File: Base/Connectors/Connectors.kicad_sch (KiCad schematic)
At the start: 18 parts, among them J1 Barrel_Jack_Switch, J2 AudioJack2_Ground, J3 AudioJack2_Ground, J4 RJ45_LED_Shielded, J5 USB_C_Receptacle_USB2.0_16P, Q1 40V

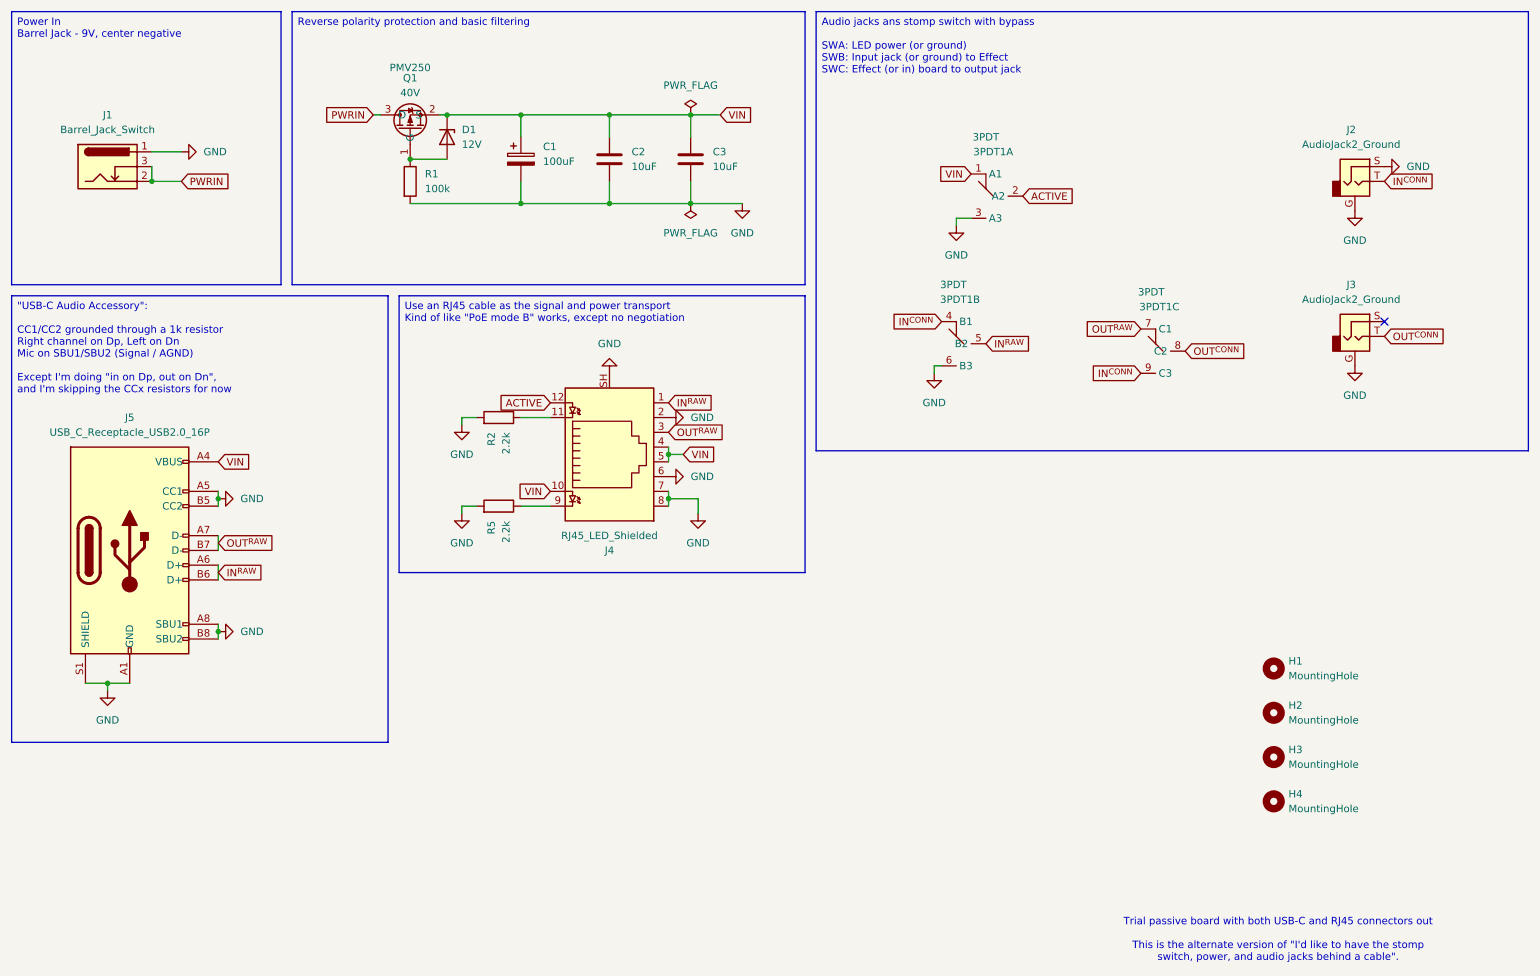
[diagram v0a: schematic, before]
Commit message: Simplify the connector testing to just a USB-C connector
This is mainly to see what that would look like, particularly for the
base that now becomes really simple and small.

The effect connector ends up being crazy large just because of the old
pin header layout.  But the point of all this is that if it works out,
we'll dispense with the pin headers, and just use the USB-C connector
"natively".

So the effects board is just a temporary thing, and the base board is
where it's at.  If the base board works well, and I can stop soldering
stomp switches, I'll be good.

Signed-off-by: Linus Torvalds <torvalds@linux-foundation.org>
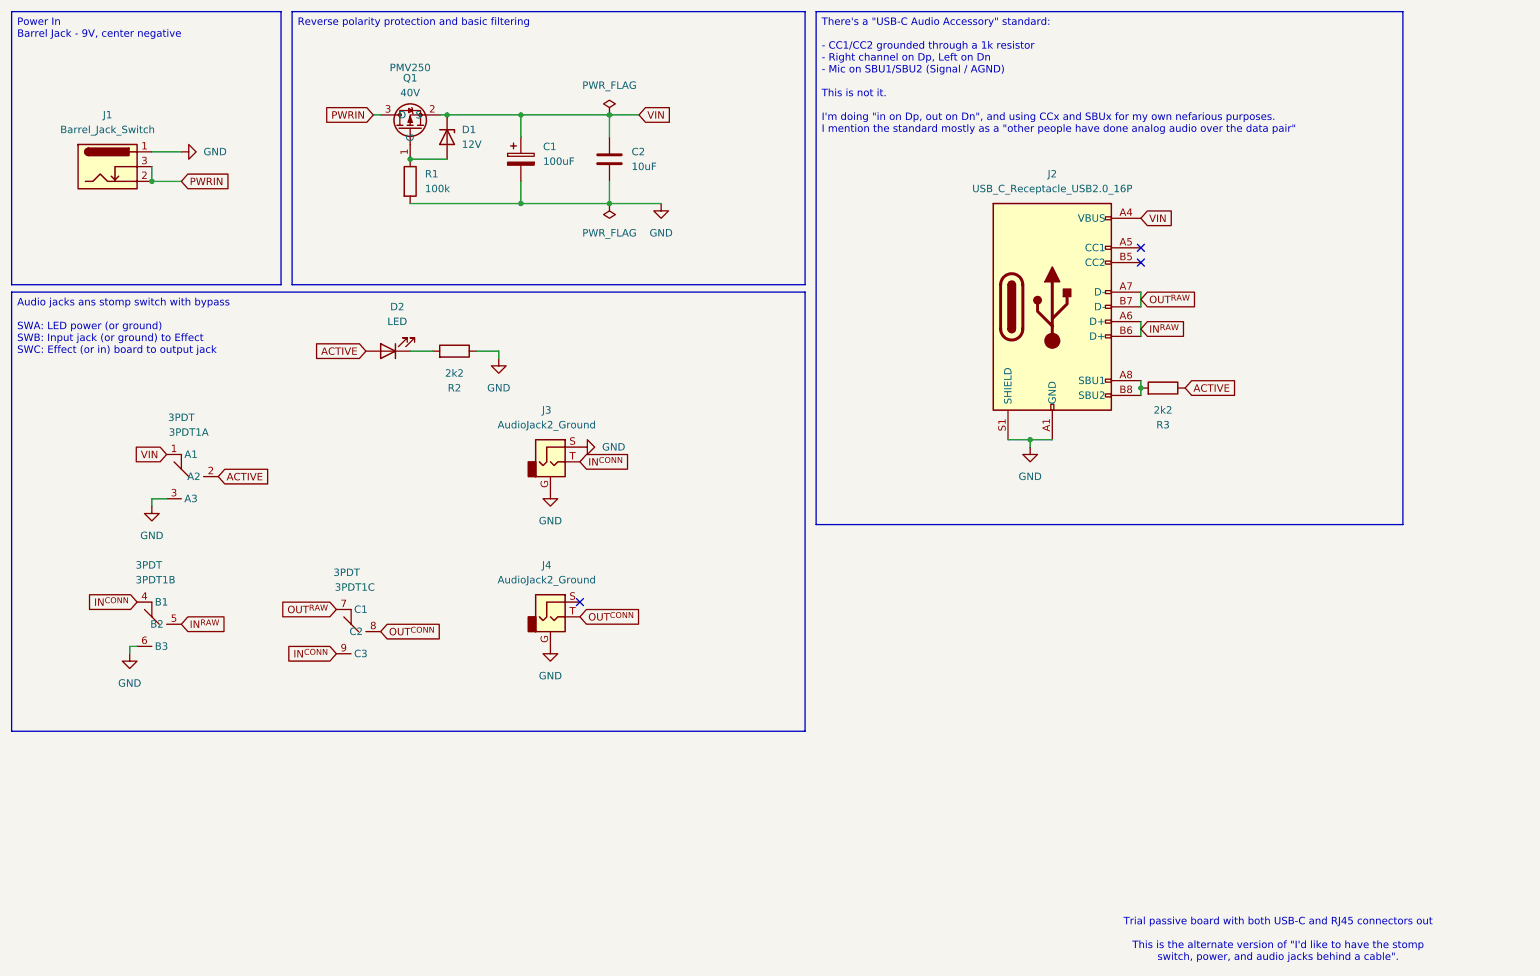
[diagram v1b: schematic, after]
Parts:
- removed C3: 10uF, Capacitor_SMD:C_1206_3216Metric_Pad1.33x1.80mm_HandSolder, symbol Device:C
- removed H1, H2, H3, H4: MountingHole, MountingHole:MountingHole_3mm, symbol Mechanical:MountingHole
- removed J4: RJ45_LED_Shielded, Connector_RJ:RJ45_Amphenol_RJHSE538X, symbol Connector:RJ45_LED_Shielded
- removed R5: 2.2k, Resistor_SMD:R_0805_2012Metric_Pad1.20x1.40mm_HandSolder, symbol Device:R
- added D2: LED, LED_THT:LED_D5.0mm, symbol Device:LED
- added R3: 2k2, Resistor_SMD:R_0805_2012Metric_Pad1.20x1.40mm_HandSolder, symbol Device:R
- R2: value 2.2k -> 2k2
- renumbered J5 to J2, J2 to J3, J3 to J4
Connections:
- net ACTIVE: now also D2.2 (A), R3.1
- net GND: now also R2.1; no longer J2.A5 (CC1), J2.A8 (SBU1), J2.B5 (CC2), J2.B8 (SBU2), R2.2
- new net: J2.A8 (SBU1), J2.B8 (SBU2), R3.2
- new net: D2.1 (K), R2.2
- no-connect marks 1 -> 3
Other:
- moved on the sheet: 3PDT1A, 3PDT1B, 3PDT1C, J2, J3, J4
